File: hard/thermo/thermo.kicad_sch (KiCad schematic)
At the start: 25 parts, among them J2 Conn_ARM_JTAG_SWD_10, J3 A-1JB, U2 nRF52832-QFxx, U3 Si7021-A20, Y1 XRCGB32M000F1H01R0, Y2 SC20S-9PF10PPM

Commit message: first pcb layout
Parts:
- added C15: 100n, Capacitor_SMD:C_0603_1608Metric_Pad1.08x0.95mm_HandSolder, symbol Device:C
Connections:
- net +BATT: now also C15.1
- net GND: now also C15.2
- net at C13.2, U2.2 (P0.00/XL1): now also Y2.2; no longer Y2.3
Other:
- moved on the sheet: C12
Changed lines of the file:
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@@
   (junction (at 201.93 89.535) (diameter 0) (color 0 0 0 0)
+  )
+  (junction (at 115.57 29.845) (diameter 0) (color 0 0 0 0)
   )
   (junction (at 184.15 38.1) (diameter 0) (color 0 0 0 0)
@@
     (stroke (width 0) (type default))
   )
+  (wire (pts (xy 66.675 108.585) (xy 66.675 109.855))
+    (stroke (width 0) (type default))
+  )
   (wire (pts (xy 176.53 55.245) (xy 191.77 55.245))
     (stroke (width 0) (type default))
@@
     (stroke (width 0) (type default))
   )
-  (wire (pts (xy 64.135 118.745) (xy 64.135 120.015))
+  (wire (pts (xy 108.585 40.005) (xy 108.585 40.64))
     (stroke (width 0) (type default))
   )
@@
     (stroke (width 0) (type default))
   )
-  (wire (pts (xy 64.135 109.855) (xy 64.135 111.125))
+  (wire (pts (xy 108.585 29.845) (xy 108.585 32.385))
     (stroke (width 0) (type default))
   )
@@
     (stroke (width 0) (type default))
   )
+  (wire (pts (xy 66.675 117.475) (xy 66.675 118.11))
+    (stroke (width 0) (type default))
+  )
   (wire (pts (xy 204.47 55.245) (xy 208.28 55.245))
     (stroke (width 0) (type default))
@@
   )
   (wire (pts (xy 132.08 29.845) (xy 132.08 43.815))
+    (stroke (width 0) (type default))
+  )
+  (wire (pts (xy 108.585 29.845) (xy 115.57 29.845))
     (stroke (width 0) (type default))
   )
@@
     )
   )
-  (symbol (lib_id "Device:C") (at 64.135 114.935 0) (unit 1)
+  (symbol (lib_id "Device:C") (at 108.585 36.195 0) (unit 1)
     (in_bom yes) (on_board yes) (dnp no)
-    (property "Reference" "C12" (at 70.485 116.205 0)
-      (effects (font (size 1.27 1.27)) (justify right))
-    )
-    (property "Value" "100n" (at 70.485 113.665 0)
-      (effects (font (size 1.27 1.27)) (justify right))
-    )
-    (property "Footprint" "Capacitor_SMD:C_0603_1608Metric_Pad1.08x0.95mm_HandSolder" (at 65.1002 118.745 0)
-      (effects (font (size 1.27 1.27)) hide)
-    )
-    (property "Datasheet" "~" (at 64.135 114.935 0)
+    (property "Reference" "C12" (at 114.935 37.465 0)
+      (effects (font (size 1.27 1.27)) (justify right))
+    )
+    (property "Value" "100n" (at 114.935 34.925 0)
+      (effects (font (size 1.27 1.27)) (justify right))
+    )
+    (property "Footprint" "Capacitor_SMD:C_0603_1608Metric_Pad1.08x0.95mm_HandSolder" (at 109.5502 40.005 0)
+      (effects (font (size 1.27 1.27)) hide)
+    )
+    (property "Datasheet" "~" (at 108.585 36.195 0)
       (effects (font (size 1.27 1.27)) hide)
     )
@@
     )
   )
-  (symbol (lib_id "power:GND") (at 64.135 120.015 0) (unit 1)
-    (in_bom yes) (on_board yes) (dnp no) (fields_autoplaced)
-    (property "Reference" "#PWR020" (at 64.135 126.365 0)
-      (effects (font (size 1.27 1.27)) hide)
-    )
-    (property "Value" "GND" (at 64.135 125.095 0)
-      (effects (font (size 1.27 1.27)))
-    )
-    (property "Footprint" "" (at 64.135 120.015 0)
-      (effects (font (size 1.27 1.27)) hide)
-    )
-    (property "Datasheet" "" (at 64.135 120.015 0)
+  (symbol (lib_id "power:GND") (at 108.585 40.64 0) (unit 1)
+    (in_bom yes) (on_board yes) (dnp no) (fields_autoplaced)
+    (property "Reference" "#PWR020" (at 108.585 46.99 0)
+      (effects (font (size 1.27 1.27)) hide)
+    )
+    (property "Value" "GND" (at 108.585 45.72 0)
+      (effects (font (size 1.27 1.27)))
+    )
+    (property "Footprint" "" (at 108.585 40.64 0)
+      (effects (font (size 1.27 1.27)) hide)
+    )
+    (property "Datasheet" "" (at 108.585 40.64 0)
       (effects (font (size 1.27 1.27)) hide)
     )
@@
     )
     (pin "1")
-    (pin "3")
+    (pin "2")
     (instances
       (project "thermo"
@@
     )
   )
+  (symbol (lib_id "power:+BATT") (at 66.675 108.585 0) (unit 1)
+    (in_bom yes) (on_board yes) (dnp no) (fields_autoplaced)
+    (property "Reference" "#PWR022" (at 66.675 112.395 0)
+      (effects (font (size 1.27 1.27)) hide)
+    )
+    (property "Value" "+BATT" (at 66.675 104.775 0)
+      (effects (font (size 1.27 1.27)))
+    )
+    (property "Footprint" "" (at 66.675 108.585 0)
+      (effects (font (size 1.27 1.27)) hide)
+    )
+    (property "Datasheet" "" (at 66.675 108.585 0)
+      (effects (font (size 1.27 1.27)) hide)
+    )
+    (pin "1")
+    (instances
+      (project "thermo"
+        (path "/1911a5bb-fcf5-4311-a6ff-b1d6aca03faf"
+          (reference "#PWR022") (unit 1)
+        )
+      )
+      (project "hello"
+        (path "/d727965f-f2fe-4d70-b3eb-f8013772d98e"
+          (reference "#PWR014") (unit 1)
+        )
+        (path "/d727965f-f2fe-4d70-b3eb-f8013772d98e/5616da9c-8e28-4bfa-9f8f-9e92a658c7c5"
+          (reference "#PWR035") (unit 1)
+        )
+      )
+    )
+  )
   (symbol (lib_id "power:GND") (at 115.57 40.005 0) (unit 1)
     (in_bom yes) (on_board yes) (dnp no) (fields_autoplaced)
@@
     )
   )
-  (symbol (lib_id "power:+BATT") (at 64.135 109.855 0) (unit 1)
-    (in_bom yes) (on_board yes) (dnp no) (fields_autoplaced)
-    (property "Reference" "#PWR019" (at 64.135 113.665 0)
-      (effects (font (size 1.27 1.27)) hide)
-    )
-    (property "Value" "+BATT" (at 64.135 106.045 0)
-      (effects (font (size 1.27 1.27)))
-    )
-    (property "Footprint" "" (at 64.135 109.855 0)
-      (effects (font (size 1.27 1.27)) hide)
-    )
-    (property "Datasheet" "" (at 64.135 109.855 0)
+  (symbol (lib_id "power:GND") (at 66.675 118.11 0) (unit 1)
+    (in_bom yes) (on_board yes) (dnp no) (fields_autoplaced)
+    (property "Reference" "#PWR019" (at 66.675 124.46 0)
+      (effects (font (size 1.27 1.27)) hide)
+    )
+    (property "Value" "GND" (at 66.675 123.19 0)
+      (effects (font (size 1.27 1.27)))
+    )
+    (property "Footprint" "" (at 66.675 118.11 0)
+      (effects (font (size 1.27 1.27)) hide)
+    )
+    (property "Datasheet" "" (at 66.675 118.11 0)
       (effects (font (size 1.27 1.27)) hide)
     )
@@
         (path "/1911a5bb-fcf5-4311-a6ff-b1d6aca03faf"
           (reference "#PWR019") (unit 1)
-        )
-      )
-      (project "hello"
-        (path "/d727965f-f2fe-4d70-b3eb-f8013772d98e"
-          (reference "#PWR014") (unit 1)
-        )
-        (path "/d727965f-f2fe-4d70-b3eb-f8013772d98e/5616da9c-8e28-4bfa-9f8f-9e92a658c7c5"
-          (reference "#PWR035") (unit 1)
         )
       )
@@
         )
       )
+    )
+  )
+  (symbol (lib_id "Device:C") (at 66.675 113.665 0) (unit 1)
+    (in_bom yes) (on_board yes) (dnp no)
+    (property "Reference" "C15" (at 73.025 114.935 0)
+      (effects (font (size 1.27 1.27)) (justify right))
+    )
+    (property "Value" "100n" (at 73.025 112.395 0)
+      (effects (font (size 1.27 1.27)) (justify right))
+    )
+    (property "Footprint" "Capacitor_SMD:C_0603_1608Metric_Pad1.08x0.95mm_HandSolder" (at 67.6402 117.475 0)
+      (effects (font (size 1.27 1.27)) hide)
+    )
+    (property "Datasheet" "~" (at 66.675 113.665 0)
+      (effects (font (size 1.27 1.27)) hide)
+    )
+    (pin "1")
+    (pin "2")
+    (instances
+      (project "thermo"
+        (path "/1911a5bb-fcf5-4311-a6ff-b1d6aca03faf"
+          (reference "C15") (unit 1)
+        )
+      )
+      (project "hello"
+        (path "/d727965f-f2fe-4d70-b3eb-f8013772d98e"
+          (reference "C5") (unit 1)
+        )
+        (path "/d727965f-f2fe-4d70-b3eb-f8013772d98e/5616da9c-8e28-4bfa-9f8f-9e92a658c7c5"
+          (reference "C15") (unit 1)
+        )
+      )

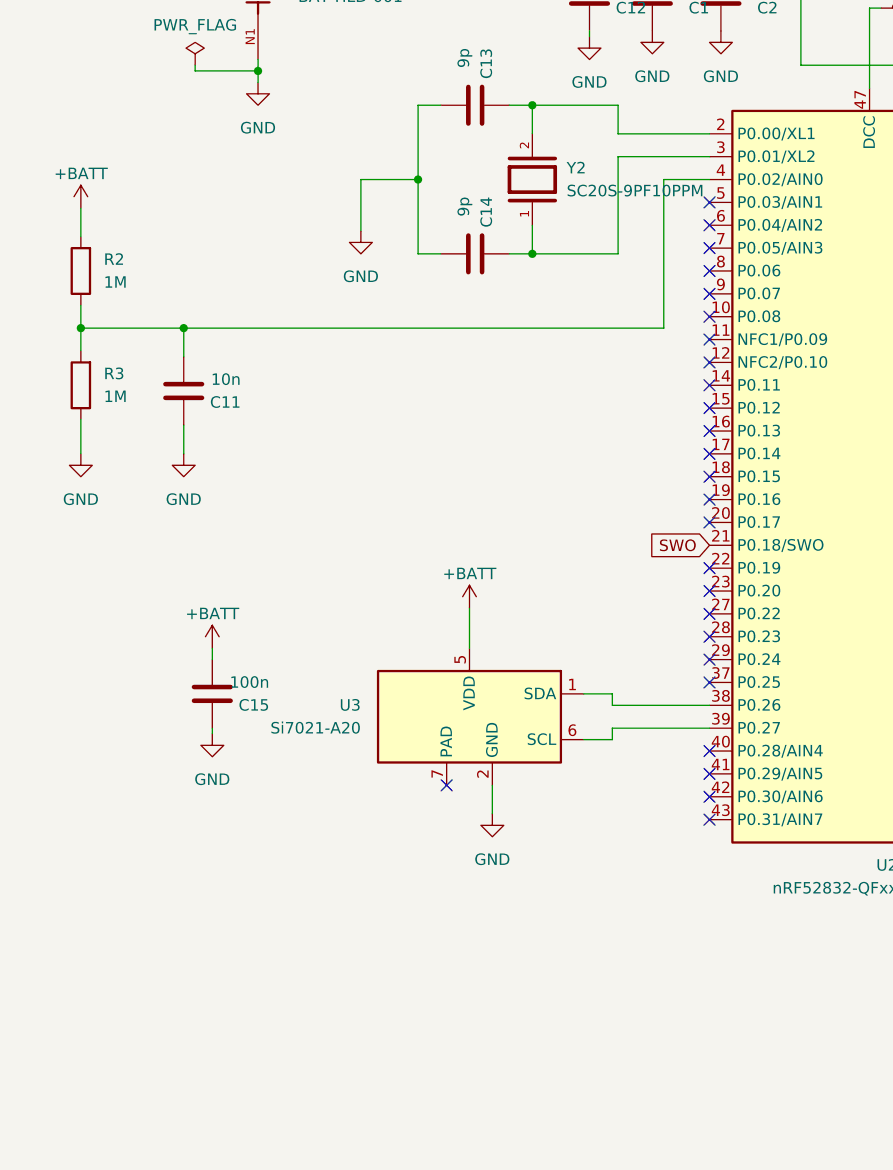
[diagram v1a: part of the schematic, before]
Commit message: - don't bother with >3.6V batt input - final layout
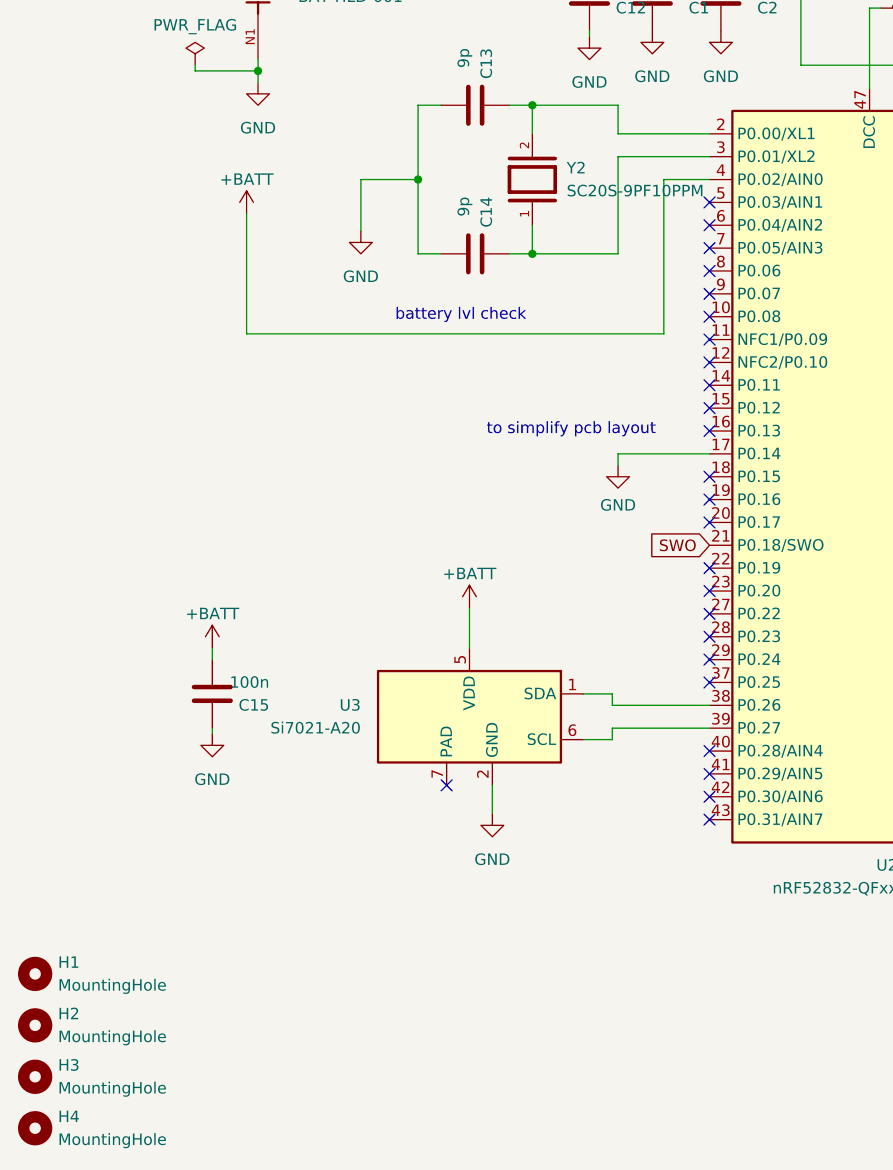
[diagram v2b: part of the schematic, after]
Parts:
- removed C11: 10n, Capacitor_SMD:C_0603_1608Metric_Pad1.08x0.95mm_HandSolder, symbol Device:C
- removed R2, R3: 1M, Resistor_SMD:R_1206_3216Metric, symbol Device:R
- added H1, H2, H3, H4: MountingHole, MountingHole:MountingHole_2.2mm_M2, symbol Mechanical:MountingHole
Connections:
- net +BATT: now also U2.4 (P0.02/AIN0)
- net GND: now also U2.17 (P0.14)
- no-connect marks 27 -> 26
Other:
- note added: "battery lvl check"
- note added: "to simplify pcb layout"

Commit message: silk screen touch-ups
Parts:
- J2: value Conn_ARM_JTAG_SWD_10 -> SWD
- J3: value A-1JB -> ANT U.FL
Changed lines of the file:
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@@
       (effects (font (size 1.27 1.27)) (justify right))
     )
-    (property "Value" "Conn_ARM_JTAG_SWD_10" (at 224.79 135.89 0)
+    (property "Value" "SWD" (at 224.79 135.89 0)
       (effects (font (size 1.27 1.27)) (justify right))
     )
@@
       (effects (font (size 1.27 1.27)))
     )
-    (property "Value" "A-1JB" (at 219.71 48.895 0)
+    (property "Value" "ANT U.FL" (at 219.71 48.895 0)
       (effects (font (size 1.27 1.27)))
     )
@@
       (effects (font (size 1.27 1.27)) (justify bottom) hide)
     )
-    (property "Description" "\nU.FL (UMCC), AMC Connector Jack, Male Pin 50Ohm Surface Mount Solder\n" (at 219.71 55.245 0)
-      (effects (font (size 1.27 1.27)) (justify bottom) hide)
-    )
+    (property "Description" " U.FL (UMCC), AMC Connector Jack, Male Pin 50Ohm Surface Mount Solder " (at 219.71 55.245 0)
+      (effects (font (size 1.27 1.27)) (justify bottom) hide)
+    )

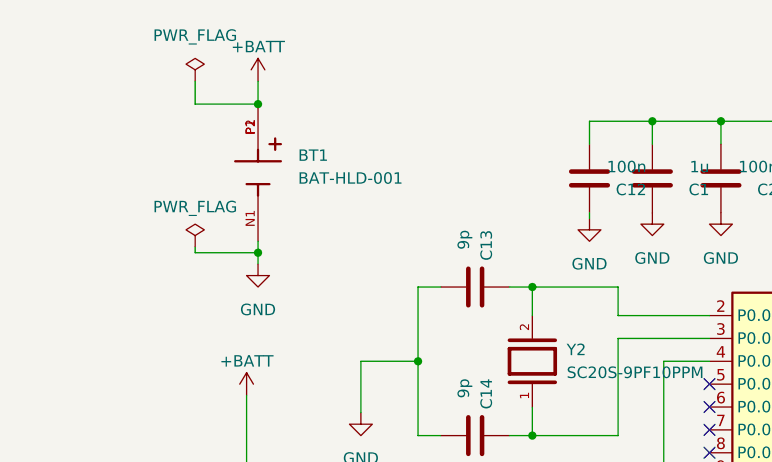
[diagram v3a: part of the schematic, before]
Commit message: - adding 3D models for nRF chip and Battery holder - stop tracking fp-info-cache file
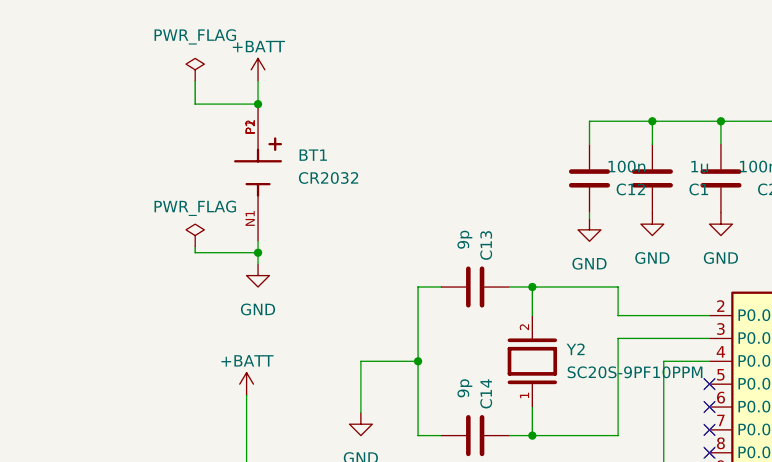
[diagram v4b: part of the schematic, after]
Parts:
- BT1: value BAT-HLD-001 -> CR2032
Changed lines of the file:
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@@
       (effects (font (size 1.27 1.27)) (justify left))
     )
-    (property "Value" "BAT-HLD-001" (at 76.2 36.195 90)
+    (property "Value" "CR2032" (at 76.2 36.195 90)
       (effects (font (size 1.27 1.27)) (justify left))
     )
